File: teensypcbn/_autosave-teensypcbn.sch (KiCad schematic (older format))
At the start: 17 parts, among them J1 CONN_26X2, J2 CONN_26X2, J3 629104190121, J4 SS-7188S-A-NF, T1 HX1198FNLT, U1 Teensy4.1

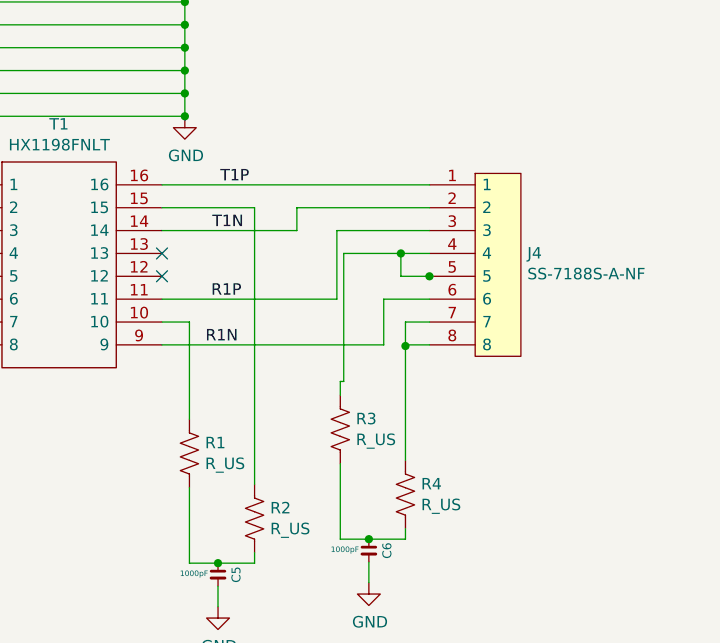
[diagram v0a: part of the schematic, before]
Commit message: routing V2
routing gestart met de juiste connector
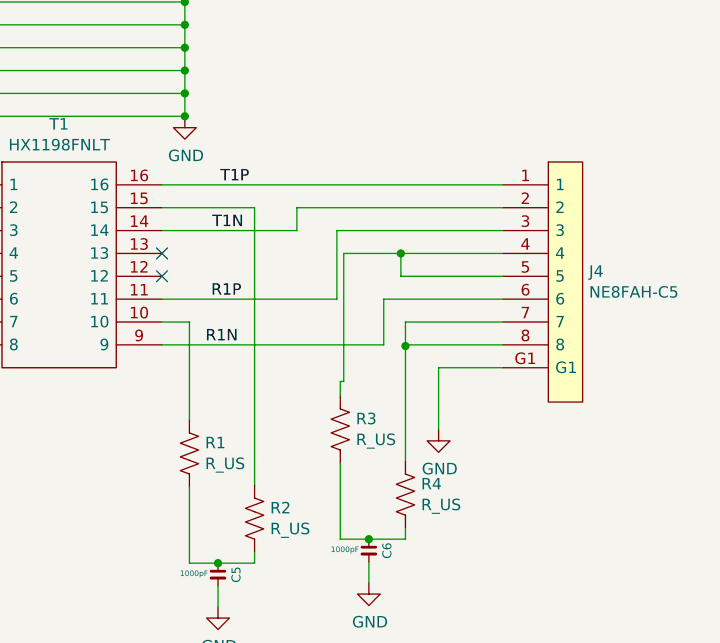
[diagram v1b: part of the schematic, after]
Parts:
- removed J4: SS-7188S-A-NF, SamacSys_Parts:SS-7188S-A-NF, symbol SamacSys_Parts:SS-7188S-A-NF
- added J4: NE8FAH-C5, SamacSys_Parts:NE8FAHC5, symbol SamacSys_Parts:NE8FAH-C5
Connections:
- net GND: now also J4.G1
- net R1N: now also J4.6
- net R1P: now also J4.3
- net T1N: now also J4.2
- net T1P: now also J4.1
- net at R3.1: now also J4.4, J4.5
- net at R4.1: now also J4.7, J4.8
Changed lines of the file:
@@
 Wire Wire Line
 	7970 4670 7970 4710
-$Comp
-L SamacSys_Parts:SS-7188S-A-NF J4
-U 1 1 5F04A257
-P 10240 4370
-F 0 "J4" H 10468 4371 50  0000 L CNN
-F 1 "SS-7188S-A-NF" H 10468 4280 50  0000 L CNN
-F 2 "SamacSys_Parts:SS-7188S-A-NF" H 10490 4620 50  0001 L CNN
-F 3 "" H 10490 4520 50  0001 L CNN
-F 4 "Bel-Stewart Cat5e RJ45 Connector Socket, Shielded, Right Angle, Through Hole" H 10490 4420 50  0001 L CNN "Description"
-F 5 "530-SS-7188S-A-NF" H 10490 4220 50  0001 L CNN "Mouser Part Number"
-F 6 "https://www.mouser.co.uk/ProductDetail/Stewart-Connector-Bel/SS-7188S-A-NF?qs=FESYatJ8odJ%252BI%2FN%2FnbWjsA%3D%3D" H 10490 4120 50  0001 L CNN "Mouser Price/Stock"
-F 7 "Bel-Stewart" H 10490 4020 50  0001 L CNN "Manufacturer_Name"
-F 8 "SS-7188S-A-NF" H 10490 3920 50  0001 L CNN "Manufacturer_Part_Number"
-	1    10240 4370
-	1    0    0    -1
-$EndComp
-Wire Wire Line
-	8870 4070 10040 4070
 Wire Wire Line
 	8870 4270 9460 4270
 Wire Wire Line
 	9460 4270 9460 4170
-Wire Wire Line
-	9460 4170 10040 4170
 NoConn ~ 8870 4370
 NoConn ~ 8870 4470
@@
 	9635 4570 9635 4270
 Wire Wire Line
-	9635 4270 10040 4270
-Wire Wire Line
 	8870 4770 9840 4770
 Wire Wire Line
 	9840 4770 9840 4570
-Wire Wire Line
-	9840 4570 10040 4570
 $Comp
 L Device:R_US R3
@@
 $EndComp
 Wire Wire Line
-	10040 4670 9935 4670
-Wire Wire Line
 	9935 4670 9935 4775
-Wire Wire Line
-	10040 4770 9940 4770
 Wire Wire Line
 	9940 4770 9940 4775
@@
 	9275 4170 9275 5380
 Wire Wire Line
-	10040 4370 9915 4370
-Wire Wire Line
 	9665 4370 9665 4930
 Wire Wire Line
@@
 	9650 4930 9650 4990
 Wire Wire Line
-	10045 4470 10040 4470
-Wire Wire Line
 	9915 4470 9915 4370
-Connection ~ 10040 4470
-Wire Wire Line
-	10040 4470 9915 4470
 Connection ~ 9915 4370
 Wire Wire Line
@@
 Wire Wire Line
 	8970 3170 8970 3270
+$Comp
+L power:GND #PWR0107
+U 1 1 5F0723BF
+P 10080 5140
+F 0 "#PWR0107" H 10080 4890 50  0001 C CNN
+F 1 "GND" H 10085 4967 50  0000 C CNN
+F 2 "" H 10080 5140 50  0001 C CNN
+F 3 "" H 10080 5140 50  0001 C CNN
+	1    10080 5140
+	1    0    0    -1
+$EndComp
+Wire Wire Line
+	9940 4770 10360 4770
+Wire Wire Line
+	9935 4670 10360 4670
+Wire Wire Line
+	8870 4070 10360 4070
+Wire Wire Line
+	9460 4170 10360 4170
+Wire Wire Line
+	9635 4270 10360 4270
+Wire Wire Line
+	9915 4370 10360 4370
+Wire Wire Line
+	9915 4470 10360 4470
+Wire Wire Line
+	9840 4570 10360 4570
+Wire Wire Line
+	10080 4870 10360 4870
+$Comp
+L SamacSys_Parts:NE8FAH-C5 J4
+U 1 1 5F148EB7
+P 10360 4070
+F 0 "J4" H 10738 3691 50  0000 L CNN
+F 1 "NE8FAH-C5" H 10738 3600 50  0000 L CNN
+F 2 "SamacSys_Parts:NE8FAHC5" H 10760 3320 50  0001 L CNN
+F 3 "https://www.neutrik.com/media/10049/download/ne8fah-c5-1.pdf?v=1" H 10760 3420 50  0001 L CNN
+F 4 "NEUTRIK - NE8FAH-C5 - CONNECTOR, RJ45, JACK, 8P8C, CAT5E" H 10760 3520 50  0001 L CNN "Description"
+F 5 "28.7" H 10510 3470 50  0001 L CNN "Height"
+F 6 "568-NE8FAH-C5" H 10760 3720 50  0001 L CNN "Mouser Part Number"
+F 7 "https://www.mouser.co.uk/ProductDetail/Neutrik/NE8FAH-C5?qs=yAJ577jGV73mSHthIeMdNw%3D%3D" H 10760 3820 50  0001 L CNN "Mouser Price/Stock"
+F 8 "Neutrik" H 10760 3920 50  0001 L CNN "Manufacturer_Name"
+F 9 "NE8FAH-C5" H 10760 4020 50  0001 L CNN "Manufacturer_Part_Number"
+	1    10360 4070
+	1    0    0    -1
+$EndComp
+Wire Wire Line
+	10080 4870 10080 5140
 $EndSCHEMATC
